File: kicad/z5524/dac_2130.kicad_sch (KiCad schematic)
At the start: 31 parts, among them U3 TL072, U5 AD5328

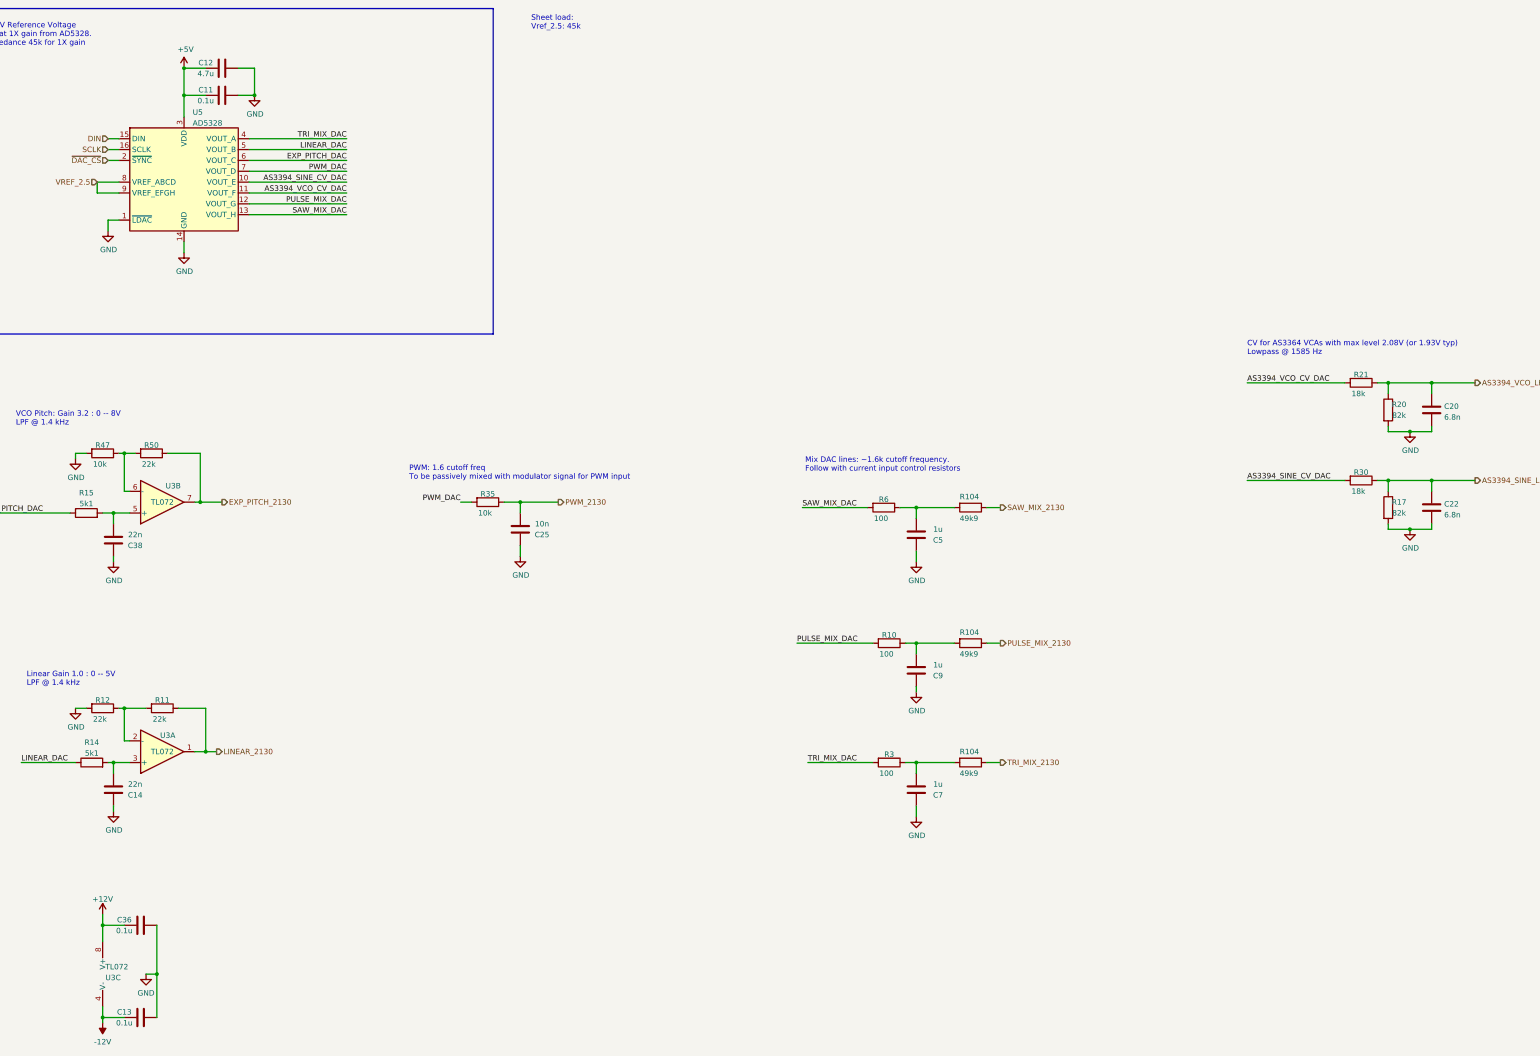
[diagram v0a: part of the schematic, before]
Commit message: reannotate geographically
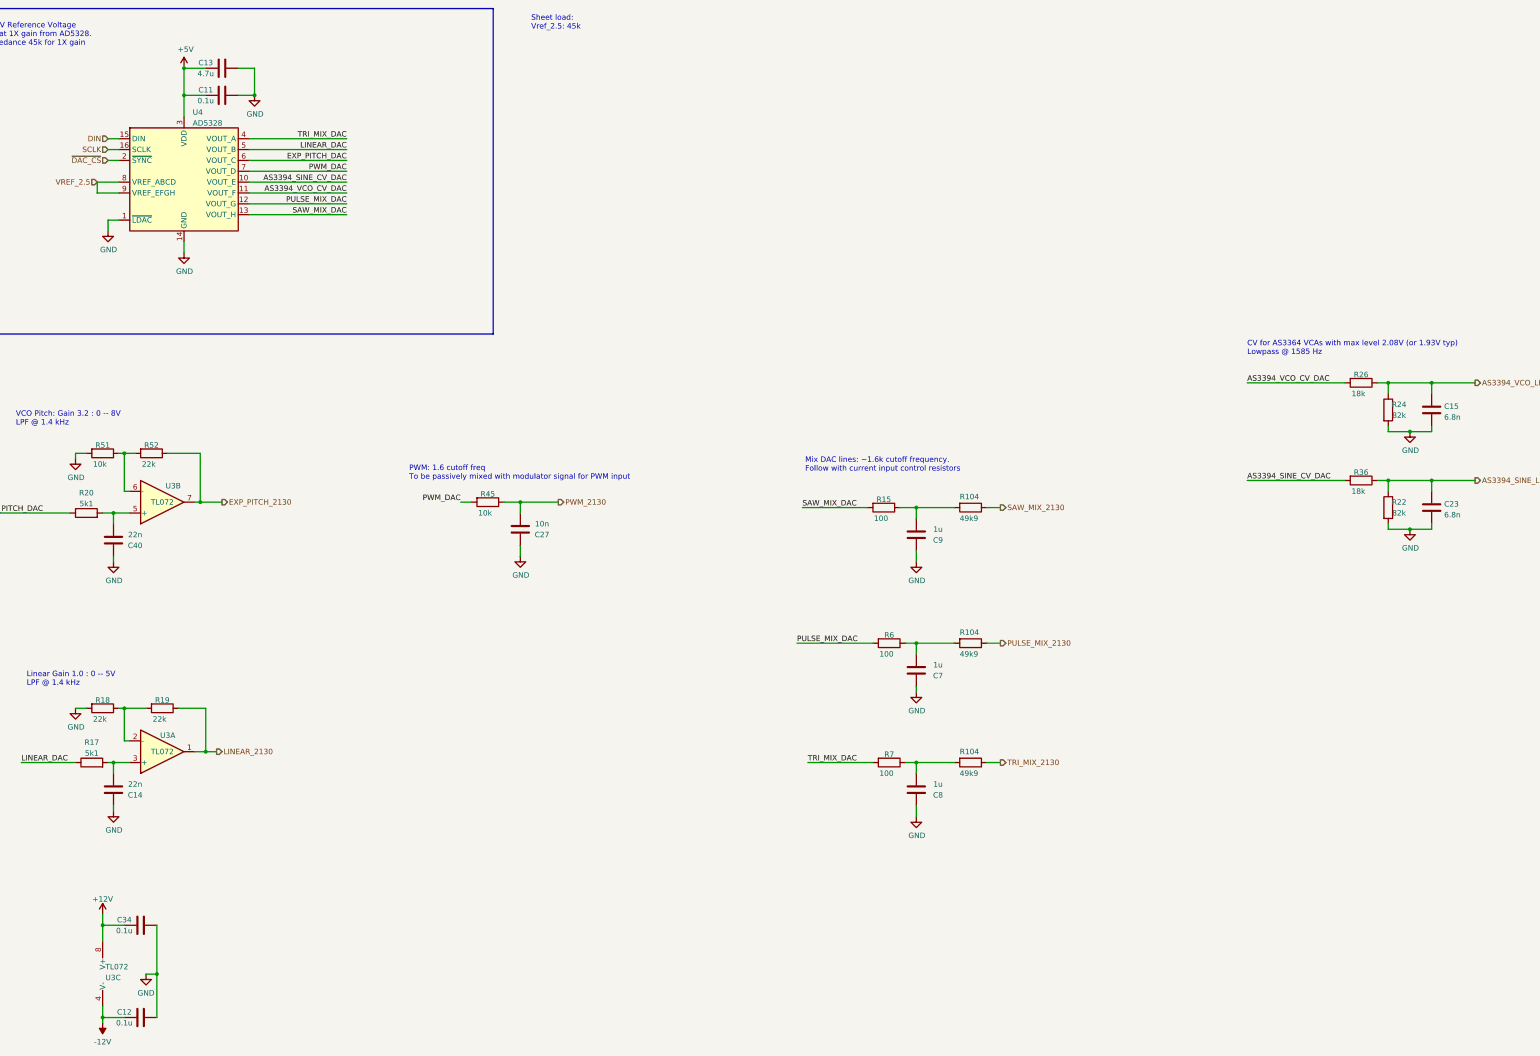
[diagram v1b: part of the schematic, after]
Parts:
- renumbered C13 to C12, C12 to C13, C20 to C15, C22 to C23, C25 to C27, C36 to C34, C38 to C40, C9 to C7, C7 to C8, C5 to C9, R6 to R15, R14 to R17, R12 to R18, R11 to R19, R15 to R20, R17 to R22, R20 to R24, R21 to R26, R30 to R36, R35 to R45, R47 to R51, R50 to R52, R10 to R6, R3 to R7, U5 to U4

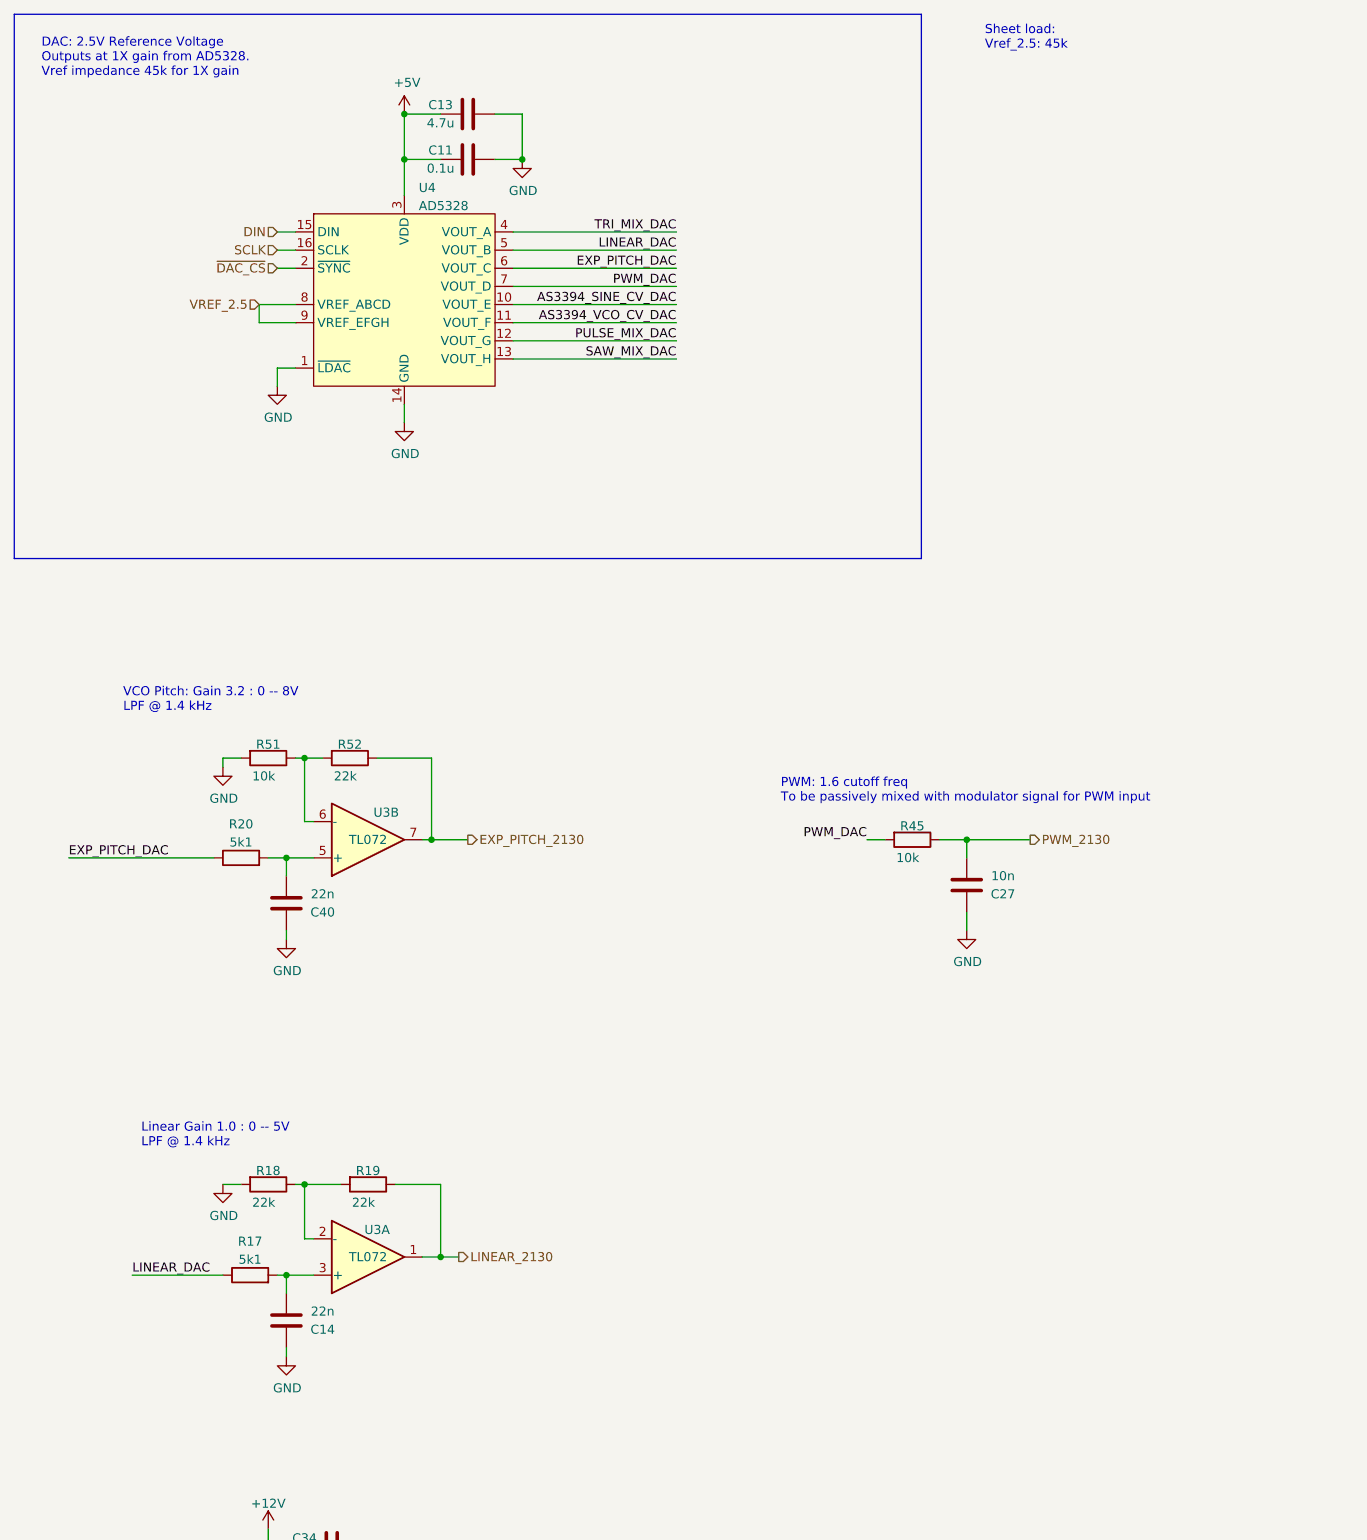
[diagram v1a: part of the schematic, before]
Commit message: updated 3394 --> 2130 FM to much deeper.  Started addressing PWM range for increased modulation
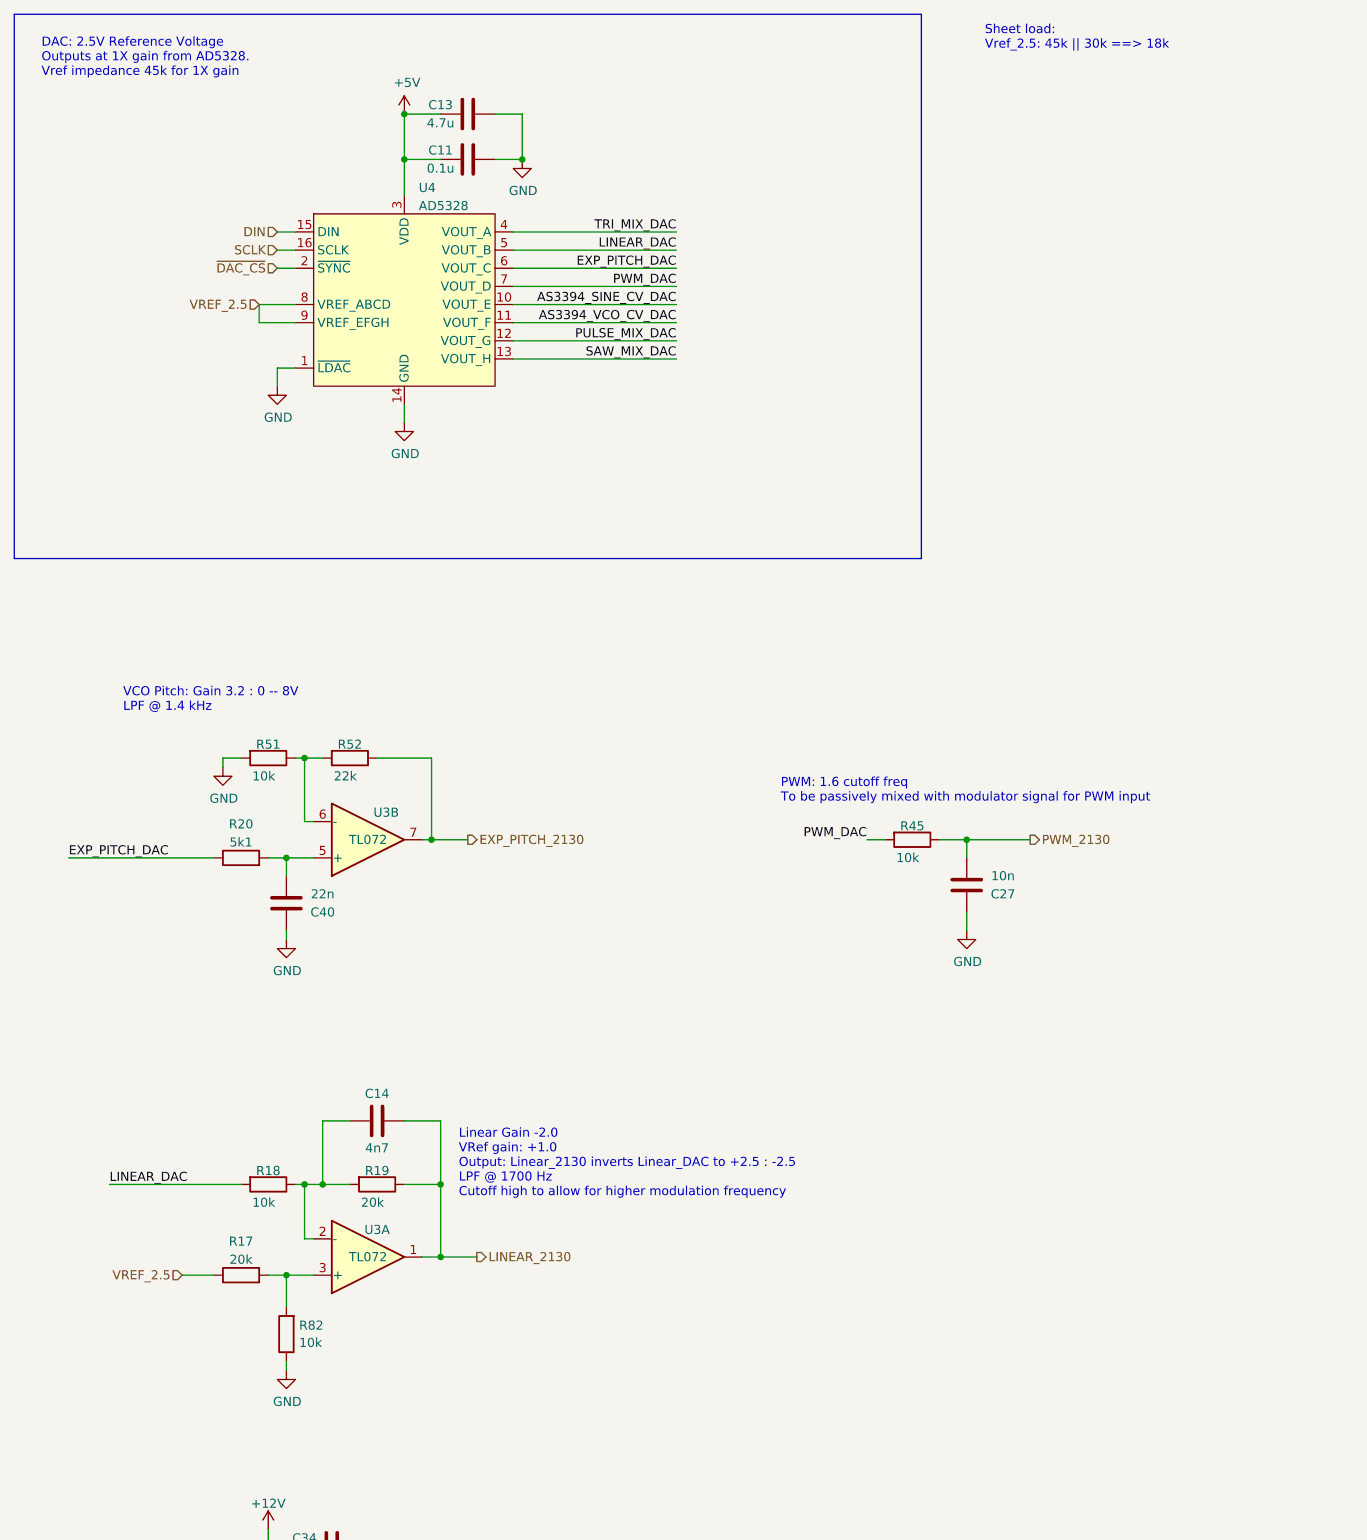
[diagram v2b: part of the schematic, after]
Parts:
- added R82: 10k, Resistor_SMD:R_0603_1608Metric, symbol Device:R
- C14: value 22n -> 4n7; LCSC C21122 -> C53987
- R17: value 5k1 -> 20k; LCSC C23186 -> (none)
- R18: value 22k -> 10k; LCSC C31850 -> (none)
- R19: value 22k -> 20k; LCSC C31850 -> (none)
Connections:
- net GND: now also R82.1; no longer C14.2, R18.2
- net LINEAR_2130: now also C14.2
- net LINEAR_DAC: now also R18.2; no longer R17.1
- net VREF_2.5: now also R17.1
- net at R17.2, U3.3 (+): now also R82.2; no longer C14.1
- net at R18.1, R19.2, U3.2 (-): now also C14.1
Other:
- note added: "Linear Gain -2.0 VRef gain: +1.0 Output: Linear_2130 inverts Linear_DAC to +2.5 : -2.5 LPF @ 1700 Hz Cutoff high to allow for higher modulation frequency"
- note added: "Sheet load: Vref_2.5: 45k || 30k ==> 18k"
- note removed: "Linear Gain 1.0 : 0 -- 5V LPF @ 1.4 kHz"
- note removed: "Sheet load: Vref_2.5: 45k"
- moved on the sheet: C14, R17, R19

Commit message: fix 2130 exp pitch input and save an opamp
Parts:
- removed C40: 22n, Capacitor_SMD:C_0603_1608Metric, symbol Device:C
- removed R20: 5k1, Resistor_SMD:R_0603_1608Metric, symbol Device:R
- removed R51: 10k, Resistor_SMD:R_0603_1608Metric, symbol Device:R
- removed R52: 22k, Resistor_SMD:R_0603_1608Metric, symbol Device:R
- added C29: 220n, Capacitor_SMD:C_0603_1608Metric, symbol Device:C
- added R108: 620, Resistor_SMD:R_0603_1608Metric, symbol Device:R
- added R109: 15k, Resistor_SMD:R_0603_1608Metric, symbol Device:R
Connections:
- net EXP_PITCH_2130: now also R109.1; no longer U3.7
- net EXP_PITCH_DAC: now also R108.2
- net GND: now also C29.2
- new net: C29.1, R108.1, R109.2
- no-connect marks 0 -> 3
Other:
- note added: "Spare"
- note added: "VCO Pitch: From 2.5V source, a 20 uA/octave source for 8 octaves gives 15625 for R. Divide this to a low impedance LPF section with a ~1200 Hz filter"
- note removed: "VCO Pitch: Gain 3.2 : 0 -- 8V LPF @ 1.4 kHz"
- moved on the sheet: C15, C23, R22, R24, R26, R36, U3B
